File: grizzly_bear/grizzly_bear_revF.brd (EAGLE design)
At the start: 76.2 x 41.3 mm, 64 parts, among them Q1 N-CHANNEL-MOSFET, Q2 N-CHANNEL-MOSFET, Q3 N-CHANNEL-MOSFET, Q4 N-CHANNEL-MOSFET, Q5 IPD90P03P4L, U1 A4940, U2 ATMEGA32U4-AU, U3 ACS714, U4 UA78L00, Y1 16MHz

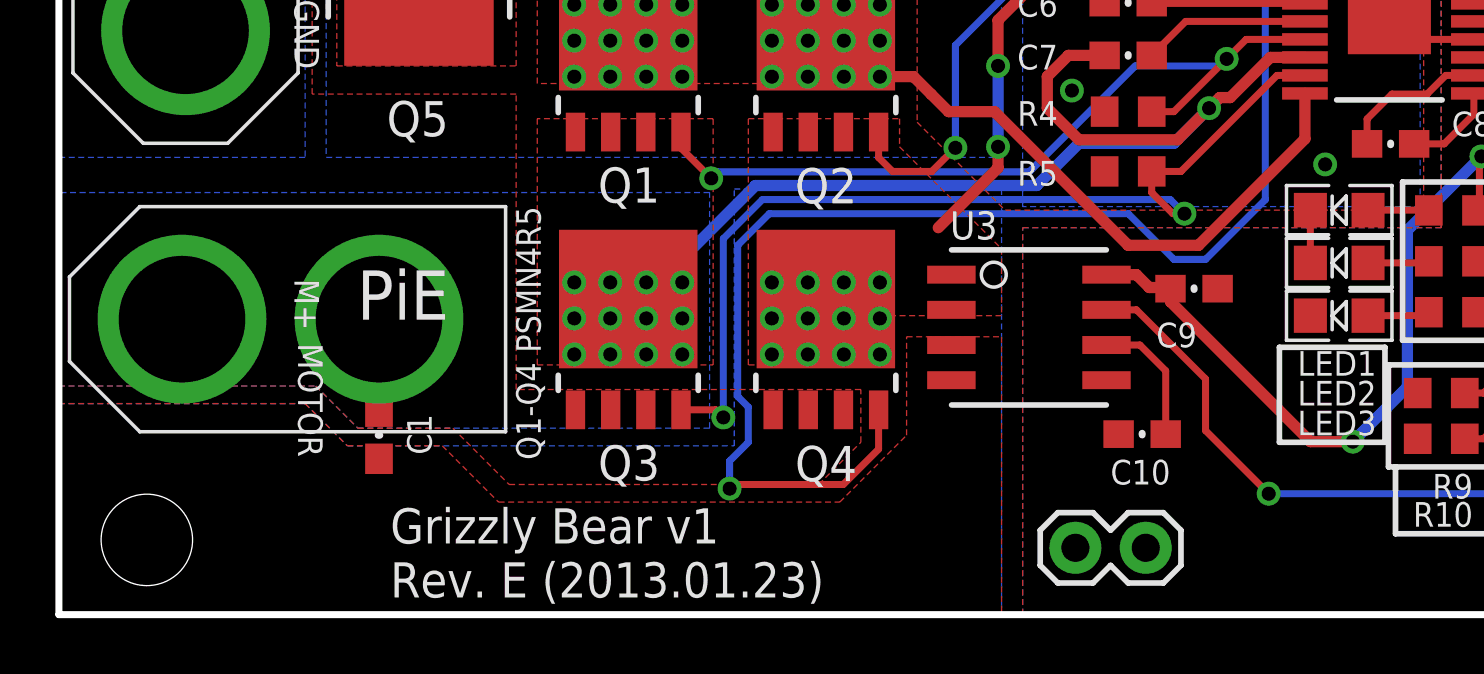
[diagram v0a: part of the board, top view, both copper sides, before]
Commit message: Edit 10/30 XT60s Hole Moved
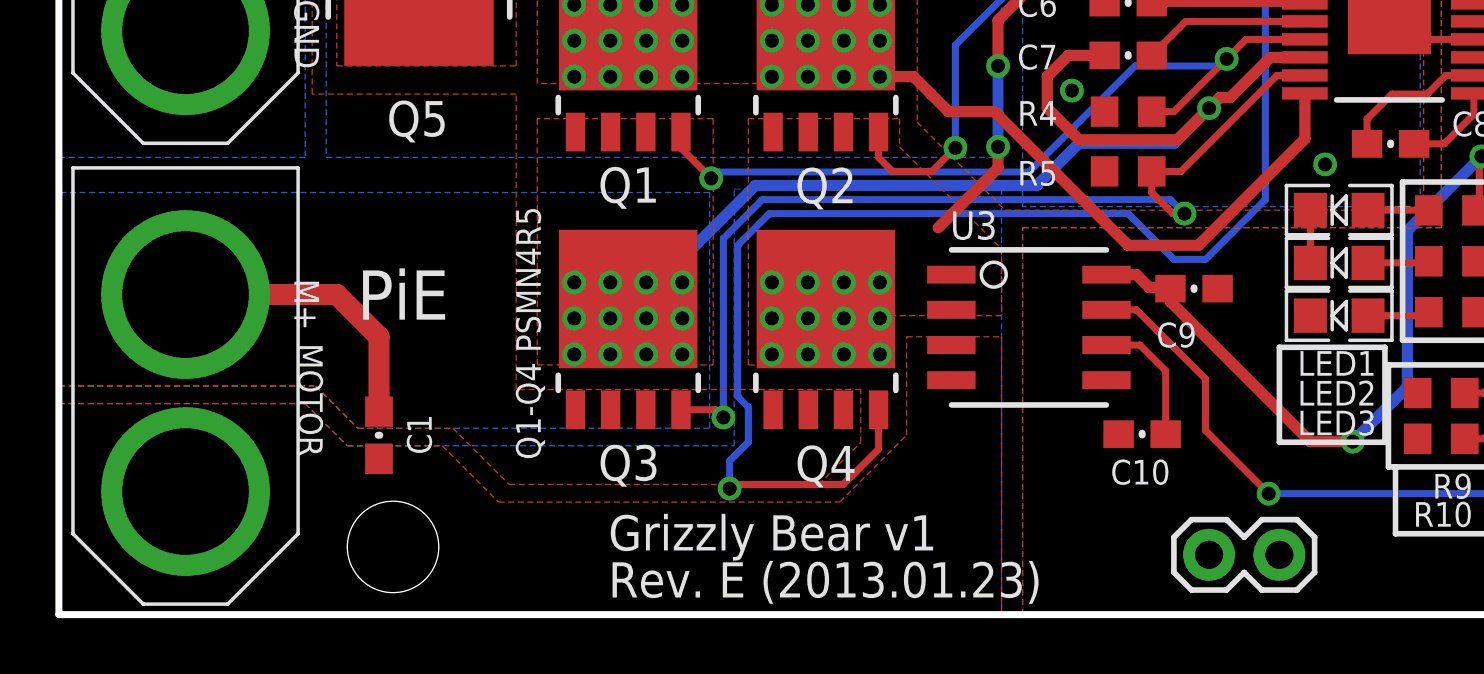
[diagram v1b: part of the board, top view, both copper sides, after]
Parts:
- moved STANDOFF4 8.89 mm to (12.1, 2.44)
- moved JP1 4.83 mm to (42.8, 2.16), turned to 180 degrees
- moved U$19 4.34 mm to (4.57, 8.00), turned to 270 degrees
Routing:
- net M+: track 42.6 -> 46.3 mm
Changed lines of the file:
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@@
 <text x="9.525" y="24.511" size="0.889" layer="21" font="vector" ratio="15" rot="SR270" align="top-center">BAT</text>
 <text x="9.525" y="7.747" size="0.889" layer="21" font="vector" ratio="15" rot="SR270" align="top-center">MOTOR</text>
-<text x="11.965" y="0.62" size="1.27" layer="21" font="vector" ratio="15">Rev. E (2013.01.23)</text>
-<text x="11.965" y="2.57" size="1.27" layer="21" font="vector" ratio="15">Grizzly Bear v1</text>
+<text x="19.839" y="0.62" size="1.27" layer="21" font="vector" ratio="15">Rev. E (2013.01.23)</text>
+<text x="19.839" y="2.316" size="1.27" layer="21" font="vector" ratio="15">Grizzly Bear v1</text>
 <text x="10.766" y="10.65" size="1.778" layer="21" font="vector" ratio="15">PiE</text>
 <text x="64.008" y="40.513" size="0.889" layer="21" font="vector" ratio="20" align="top-left">Addr Select</text>
@@
 <attribute name="VALUE" x="8.509" y="16.256" size="0.889" layer="27" font="vector" ratio="20"/>
 </element>
-<element name="JP1" library="pie" package="1X02" value="GND" x="37.973" y="2.413" smashed="yes">
-<attribute name="VALUE" x="41.91" y="1.143" size="0.889" layer="27" font="vector" ratio="20"/>
+<element name="JP1" library="pie" package="1X02" value="GND" x="42.799" y="2.159" smashed="yes" rot="R180">
+<attribute name="VALUE" x="38.862" y="3.429" size="0.889" layer="27" font="vector" ratio="20" rot="R180"/>
 </element>
 <element name="SJ1" library="pie" package="SJ_2S-NO" value="SOLDERJUMPERNO" x="60.579" y="10.414" smashed="yes" rot="R270"/>
@@
 <attribute name="PARTNUMBER" value="PRT-10474 " x="4.572" y="24.638" size="1.778" layer="27" rot="R270" display="off"/>
 </element>
-<element name="U$19" library="pie" package="XT60CONNECTOR" value="XT60CONNECTOR" x="8.001" y="10.668" rot="R180">
-<attribute name="PARTNUMBER" value="PRT-10474 " x="8.001" y="10.668" size="1.778" layer="27" rot="R180" display="off"/>
+<element name="U$19" library="pie" package="XT60CONNECTOR" value="XT60CONNECTOR" x="4.572" y="8.001" rot="R270">
+<attribute name="PARTNUMBER" value="PRT-10474 " x="4.572" y="8.001" size="1.778" layer="27" rot="R270" display="off"/>
 </element>
 <element name="STANDOFF1" library="pie" package="STAND-OFF" value="STAND-OFF" x="3.175" y="38.25875"/>
@@
 <element name="U$1" library="pie" package="OSHW-LOGO-L" value="" x="10.16" y="36.83" rot="MR0"/>
 <element name="STANDOFF3" library="pie" package="STAND-OFF" value="STAND-OFF" x="74.295" y="38.25875"/>
-<element name="STANDOFF4" library="pie" package="STAND-OFF" value="STAND-OFF" x="3.175" y="2.69875"/>
+<element name="STANDOFF4" library="pie" package="STAND-OFF" value="STAND-OFF" x="12.065" y="2.44475"/>
 </elements>
 <signals>
@@
 <wire x1="37.825" y1="8.465" x2="41.837" y2="11.77" width="0" layer="19" extent="1-1"/>
 <wire x1="38.263" y1="6.518" x2="37.825" y2="8.465" width="0" layer="19" extent="1-1"/>
-<wire x1="39.243" y1="2.413" x2="38.263" y2="6.518" width="0" layer="19" extent="1-1"/>
-<wire x1="36.703" y1="2.413" x2="39.243" y2="2.413" width="0" layer="19" extent="1-1"/>
+<wire x1="41.529" y1="2.159" x2="38.263" y2="6.518" width="0" layer="19" extent="1-1"/>
+<wire x1="44.069" y1="2.159" x2="41.529" y2="2.159" width="0" layer="19" extent="1-1"/>
 <wire x1="39.37" y1="36.83" x2="53.34" y2="36.83" width="0" layer="19" extent="1-1"/>
 <wire x1="34.359" y1="35.052" x2="39.37" y2="36.83" width="0" layer="19" extent="16-16"/>
@@
 <wire x1="10.033" y1="11.557" x2="11.557" y2="10.033" width="0.762" layer="1"/>
 <wire x1="11.557" y1="7.327" x2="11.557" y2="10.033" width="0.762" layer="1"/>
-<wire x1="11.557" y1="10.668" x2="10.033" y2="11.557" width="0.762" layer="1"/>
+<wire x1="4.572" y1="11.557" x2="10.033" y2="11.557" width="0.762" layer="1"/>
 </signal>
 <signal name="ISENSE">

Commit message: Grizzly Revision B 11/10/13
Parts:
- moved C1 3.00 mm to (14.6, 6.48)
- moved JP3 1.91 mm to (38.7, 36.9)
- moved JP6 1.91 mm to (57.8, 36.9)
- moved SV1 1.91 mm to (66.7, 36.9)
- moved JP4 1.91 mm to (48.9, 36.9)
- moved SJ2 1.78 mm to (32.1, 35.1)
- moved R15 1.40 mm to (54.0, 32.8)
- moved STANDOFF2 1.04 mm to (73.4, 2.79)
- moved STANDOFF3 0.90 mm to (73.4, 38.1)
- moved STANDOFF4 0.52 mm to (11.7, 2.79)
- moved STANDOFF1 0.20 mm to (3.05, 38.1)
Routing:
- net M+: track 46.3 -> 48.8 mm, vias 13 -> 12
- net ENC1: track 38.0 -> 39.8 mm
- net SCL: track 24.6 -> 26.2 mm
- net MOSI: track 30.0 -> 31.5 mm
- net ENC2: track 31.3 -> 32.8 mm
- net DIP4: track 13.9 -> 15.1 mm
- net SCK: track 20.2 -> 21.1 mm
- net SDA: track 20.6 -> 21.5 mm
- net DIP3: track 34.2 -> 35.0 mm
- net DIP5: track 35.1 -> 35.9 mm
- net DIP2: track 30.6 -> 31.4 mm
- net DIP1: track 32.8 -> 33.6 mm
- net MISO: track 23.7 -> 24.3 mm
- net GND: vias 10 -> 11
- added copper zone on layer 1, net 5V
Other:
- board text added: "Grizzly Bear v2"
- board text added: "Rev. B (2013.11.10)"
- board text removed: "Grizzly Bear v1"
- board text removed: "Rev. E (2013.01.23)"

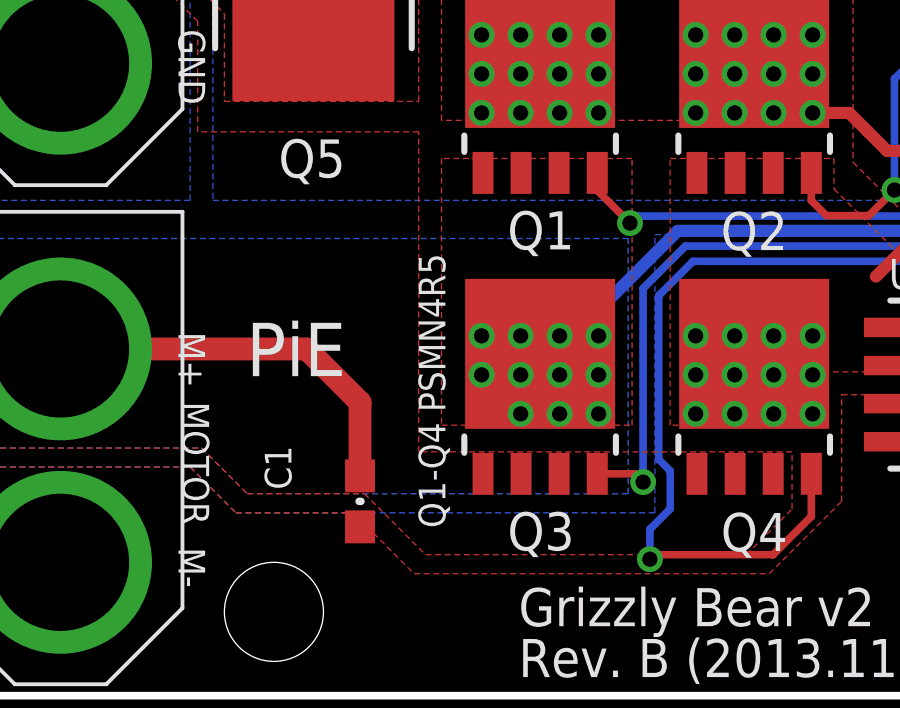
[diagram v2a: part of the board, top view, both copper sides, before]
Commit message: Grizzly Revision 11/11/13
Via added, moved "Q1-Q4..." to tValue layer, Copyright info moved
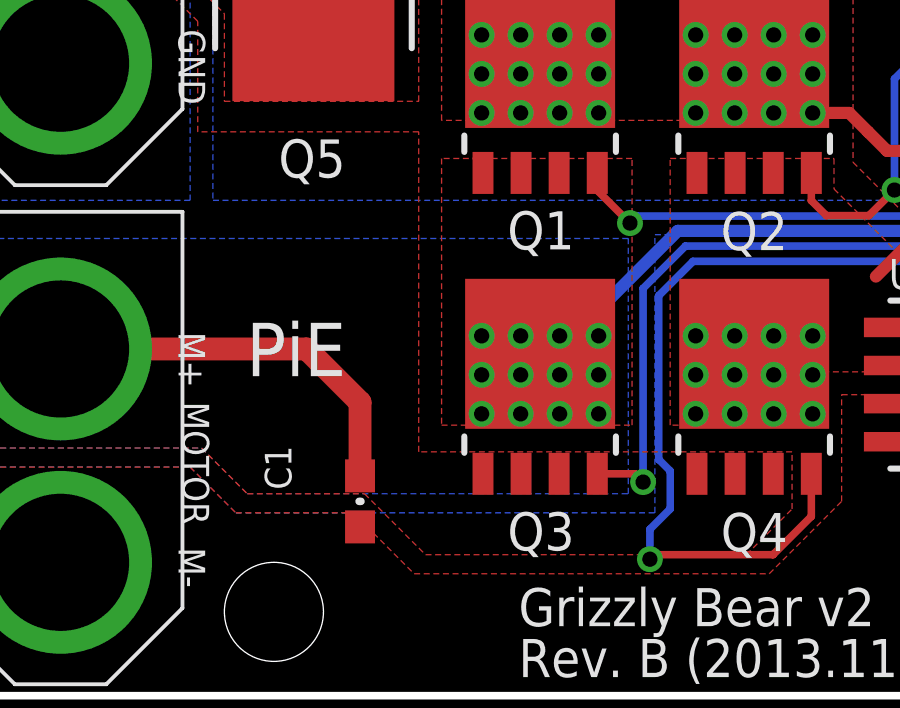
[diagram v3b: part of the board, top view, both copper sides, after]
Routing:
- net M+: vias 12 -> 13
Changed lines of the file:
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@@
 <wire x1="48.26" y1="2.921" x2="54.229" y2="2.921" width="0.2032" layer="21"/>
 <wire x1="54.229" y1="2.921" x2="54.229" y2="5.334" width="0.2032" layer="21"/>
-<text x="17.399" y="5.588" size="0.889" layer="21" font="vector" ratio="20" rot="R90">Q1-Q4 PSMN4R5</text>
+<text x="17.399" y="5.588" size="0.889" layer="27" font="vector" ratio="20" rot="R90">Q1-Q4 PSMN4R5</text>
 <text x="52.451" y="14.351" size="0.889" layer="21" font="vector" ratio="20">330</text>
 <text x="54.61" y="4.064" size="0.889" layer="21" font="vector" ratio="20">10k</text>
@@
 Pioneers in Engineering
 All rights reserved.</text>
-<text x="31.75" y="40.386" size="1.016" layer="22" font="vector" ratio="15" rot="SMR270">Design by:
+<text x="30.2514" y="40.386" size="1.016" layer="22" font="vector" ratio="15" rot="SMR270">Design by:
     Jay Chenn,
     Keegan Mann,
@@
 <wire x1="19.907" y1="9.395" x2="19.907" y2="10.695" width="0" layer="19" extent="1-1"/>
 <wire x1="14.5542" y1="9.779" x2="18.607" y2="10.695" width="0" layer="19" extent="1-1"/>
+<via x="18.607" y="9.395" extent="1-16" drill="0.508"/>
 </signal>
 <signal name="ISENSE">

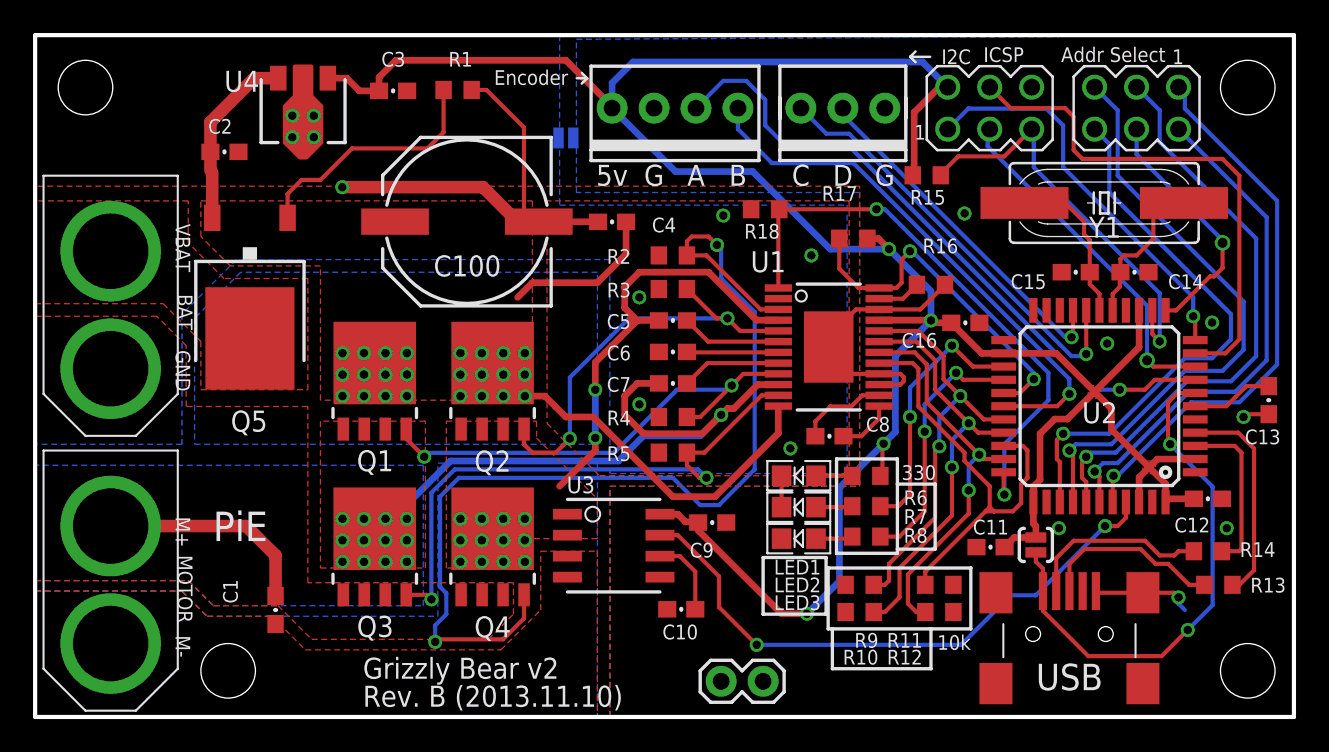
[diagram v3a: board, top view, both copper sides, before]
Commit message: Grizzly Revision B 11/11/13
Revision date/Copyright info updated, Unrouted trace moved to the right.
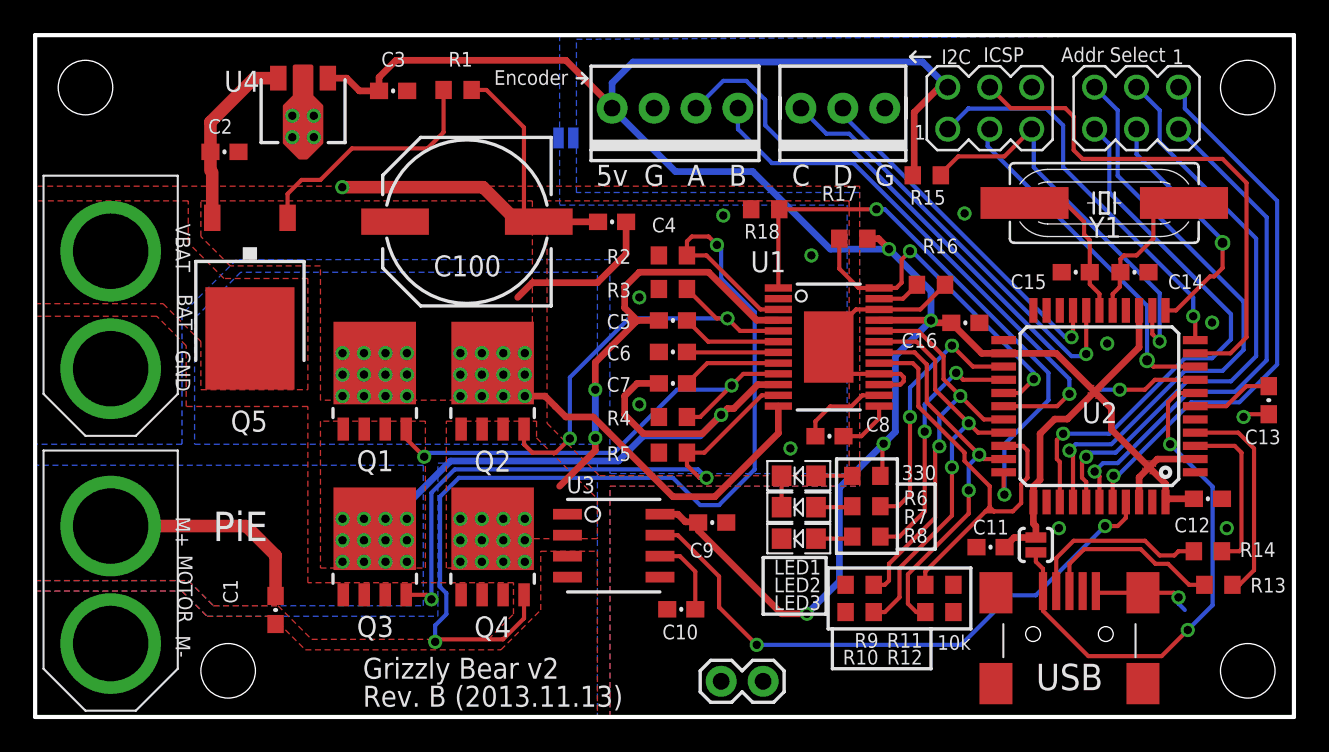
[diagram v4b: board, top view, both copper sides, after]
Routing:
- net MOSI: track 31.5 -> 32.0 mm
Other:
- board text added: "Design by: Jay Chenn, Keegan Mann, Robert Ou, Jeffrey Jacinto This design is open source hardware. For more information, visit pioneers.berkeley.edu/opensource"
- board text added: "Rev. B (2013.11.13)"
- board text removed: "Design by: Jay Chenn, Keegan Mann, Robert Ou This design is open source hardware. For more information, visit pioneers.berkeley.edu/opensource"
- board text removed: "Rev. B (2013.11.10)"
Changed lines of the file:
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@@
 <text x="9.525" y="24.511" size="0.889" layer="21" font="vector" ratio="15" rot="SR270" align="top-center">BAT</text>
 <text x="9.525" y="7.747" size="0.889" layer="21" font="vector" ratio="15" rot="SR270" align="top-center">MOTOR</text>
-<text x="19.839" y="0.62" size="1.27" layer="21" font="vector" ratio="15">Rev. B (2013.11.10)</text>
+<text x="19.839" y="0.62" size="1.27" layer="21" font="vector" ratio="15">Rev. B (2013.11.13)</text>
 <text x="19.839" y="2.316" size="1.27" layer="21" font="vector" ratio="15">Grizzly Bear v2</text>
 <text x="10.766" y="10.65" size="1.778" layer="21" font="vector" ratio="15">PiE</text>
@@
     Jay Chenn,
     Keegan Mann,
-    Robert Ou
+    Robert Ou,
+    Jeffrey Jacinto
 This design is open
 source hardware.
@@
 <contactref element="JP6" pad="4"/>
 <contactref element="U2" pad="10"/>
-<wire x1="70.22800625" y1="22.012" x2="72.05" y2="22.012" width="0.254" layer="1"/>
-<wire x1="72.05" y1="22.012" x2="72.898" y2="22.86" width="0.254" layer="1"/>
-<wire x1="72.898" y1="22.86" x2="72.898" y2="32.766" width="0.254" layer="1"/>
-<wire x1="63.3984" y1="33.782" x2="62.865" y2="34.3154" width="0.254" layer="1"/>
 <wire x1="62.865" y1="34.3154" x2="62.865" y2="36.3474" width="0.254" layer="1"/>
 <wire x1="62.865" y1="36.3474" x2="62.357" y2="36.8554" width="0.254" layer="1"/>
 <wire x1="62.357" y1="36.8554" x2="59.055" y2="36.8554" width="0.254" layer="1"/>
 <wire x1="59.055" y1="36.8554" x2="57.785" y2="38.1254" width="0.254" layer="1"/>
-<wire x1="72.898" y1="32.766" x2="71.882" y2="33.782" width="0.254" layer="1"/>
 <wire x1="71.882" y1="33.782" x2="63.3984" y2="33.782" width="0.254" layer="1"/>
+<wire x1="70.22800625" y1="22.012" x2="72.3548" y2="22.012" width="0.254" layer="1"/>
+<wire x1="72.3548" y1="22.012" x2="73.3298" y2="22.987" width="0.254" layer="1"/>
+<wire x1="73.3298" y1="22.987" x2="73.3298" y2="32.3342" width="0.254" layer="1"/>
+<wire x1="73.3298" y1="32.3342" x2="71.882" y2="33.782" width="0.254" layer="1"/>
+<wire x1="63.3984" y1="33.782" x2="62.865" y2="34.3154" width="0.254" layer="1"/>
 </signal>
 <signal name="RESET">
@@
 <wire x1="14.5542" y1="7.327" x2="14.5542" y2="9.779" width="0.762" layer="1"/>
 <wire x1="14.5542" y1="9.779" x2="12.7762" y2="11.557" width="0.762" layer="1"/>
-<wire x1="19.922" y1="17.425" x2="21.192" y2="17.425" width="0" layer="19" extent="1-1"/>
-<wire x1="18.652" y1="17.425" x2="19.922" y2="17.425" width="0" layer="19" extent="1-1"/>
-<wire x1="25.146" y1="15.494" x2="21.192" y2="17.425" width="0" layer="19" extent="1-16"/>
-<wire x1="22.507" y1="11.995" x2="22.606" y2="12.954" width="0" layer="19" extent="16-16"/>
-<wire x1="22.507" y1="10.695" x2="22.507" y2="11.995" width="0" layer="19" extent="1-1"/>
-<wire x1="21.207" y1="10.695" x2="22.507" y2="10.695" width="0" layer="19" extent="1-1"/>
-<wire x1="20.557" y1="11.395" x2="21.207" y2="10.695" width="0" layer="19" extent="1-1"/>
-<wire x1="21.207" y1="11.995" x2="20.557" y2="11.395" width="0" layer="19" extent="1-1"/>
-<wire x1="19.907" y1="11.995" x2="20.557" y2="11.395" width="0" layer="19" extent="1-1"/>
-<wire x1="19.907" y1="10.695" x2="20.557" y2="11.395" width="0" layer="19" extent="1-1"/>
-<wire x1="21.207" y1="9.395" x2="21.207" y2="10.695" width="0" layer="19" extent="1-1"/>
-<wire x1="22.507" y1="9.395" x2="22.507" y2="10.695" width="0" layer="19" extent="1-1"/>
-<wire x1="18.607" y1="10.695" x2="19.907" y2="10.695" width="0" layer="19" extent="1-1"/>
-<wire x1="18.607" y1="11.995" x2="19.907" y2="11.995" width="0" layer="19" extent="1-1"/>
-<wire x1="19.907" y1="9.395" x2="19.907" y2="10.695" width="0" layer="19" extent="1-1"/>
-<wire x1="14.5542" y1="9.779" x2="18.607" y2="10.695" width="0" layer="19" extent="1-1"/>
 <via x="18.607" y="9.395" extent="1-16" drill="0.508"/>
 </signal>
